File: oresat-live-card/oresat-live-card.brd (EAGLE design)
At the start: 99.8 x 94.6 mm, 323 parts, among them J1 ORESAT-DEBUG-CONNECTOR-CARD, J100 DM3BT-DSF-PEJS, J102 FTSH-105-XX-X-DV-K, J2 SM06B-SRSS-TB(LF)(SN), J4 TFM-120-01-L-D-RA, Q1 MMBT2907, Q2 PMV45EN, Q3 DMP2240UDM, Q4 PMV45EN, Q5 MOSFET-PCH-SOT23-6, Q6 MOSFET-PCH-SOT23-6, U1 RCLAMP0504FB, U10 TLVH431, U11 TCAN330, U12 MIC842LYC5, U13 MIC842LYC5, U14 MAX4211FETE, U15 TPS62112, U16 MAX7310ATE, U17 25AAXX, U18 RCLAMP0504FB, U19 TQP9111, U2 TPS2051CDBVR, U3 THGBMJG7C2LBAU8, U4 SN74LVC1G07DCK, U5 TPS62112, U6 SN74LVC1G32QDBVRQ1, U7 OSD3358-512M-BSM, U8 MIC94090YC6-TR, Y1 24MHz, Y2 ABS07-32.768KHZ-T

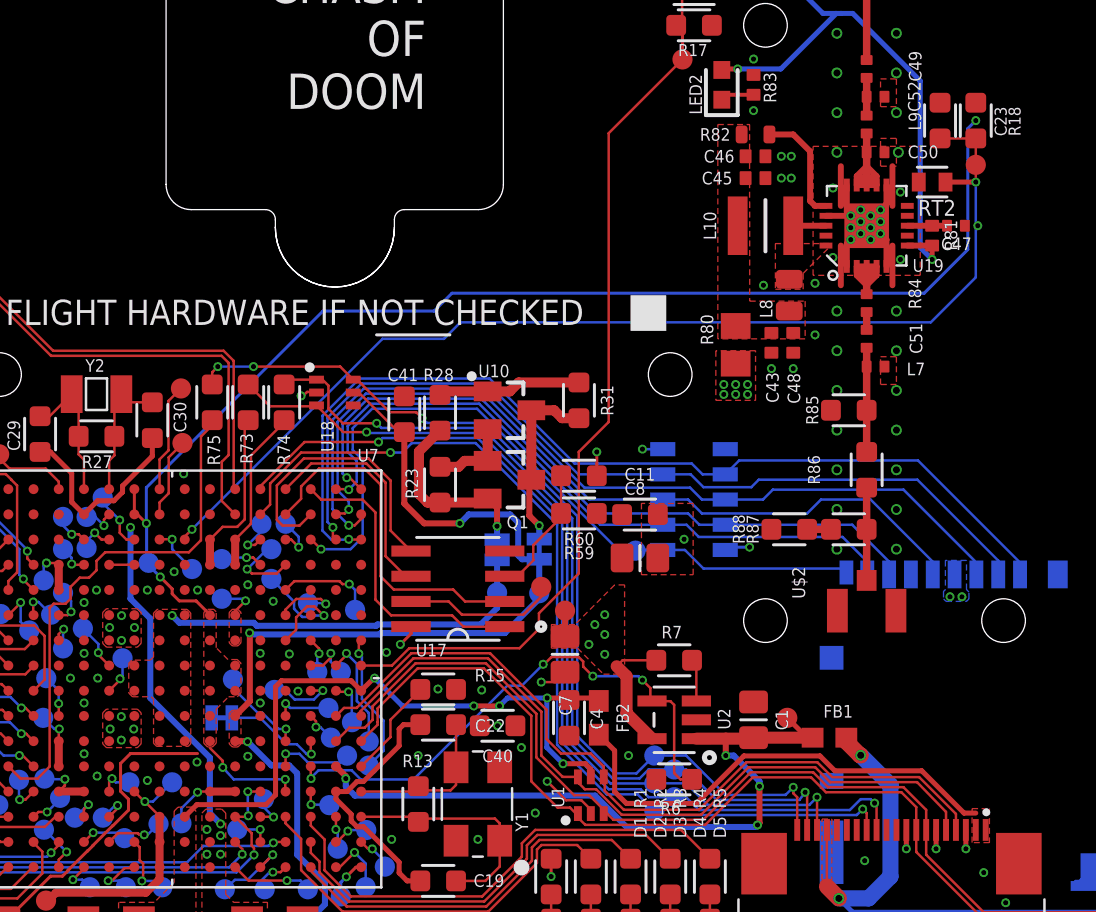
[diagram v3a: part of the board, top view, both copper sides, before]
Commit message: modified thermistor routing to not go though vias after it was moved
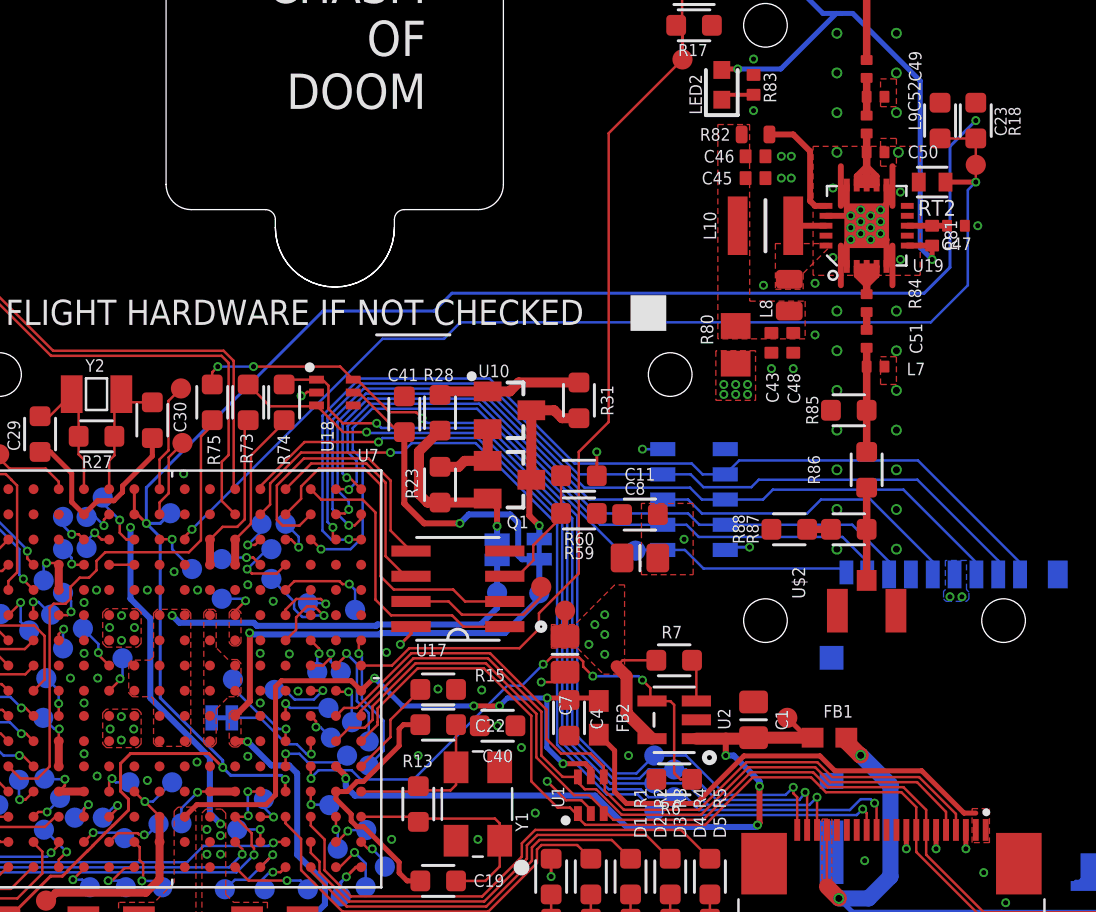
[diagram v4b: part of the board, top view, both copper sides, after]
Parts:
- moved TP171 2.73 mm to (41.6, 25.9)
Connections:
- new net 1.8V-A: C24.1, C25.1, C26.1, TP171.P$1, TP8.P$1, U7.A7, U7.B7, U7.N13
- net 1.8V: no longer C24.1, C25.1, C26.1, TP171.P$1, TP8.P$1, U7.A7, U7.B7, U7.N13
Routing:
- net 1.8V-A: track 0.00 -> 96.2 mm, vias 0 -> 4
- net 1.8V: track 86.8 -> 0.00 mm, vias 5 -> 0
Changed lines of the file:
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@@
 <layer number="13" name="Route13" color="4" fill="5" visible="no" active="no"/>
 <layer number="14" name="Route14" color="1" fill="6" visible="no" active="no"/>
-<layer number="15" name="Route15" color="14" fill="1" visible="no" active="yes"/>
-<layer number="16" name="Bottom" color="1" fill="1" visible="no" active="yes"/>
+<layer number="15" name="Route15" color="14" fill="1" visible="yes" active="yes"/>
+<layer number="16" name="Bottom" color="1" fill="1" visible="yes" active="yes"/>
 <layer number="17" name="Pads" color="2" fill="1" visible="yes" active="yes"/>
 <layer number="18" name="Vias" color="2" fill="1" visible="yes" active="yes"/>
@@
 <layer number="20" name="Dimension" color="15" fill="1" visible="yes" active="yes"/>
 <layer number="21" name="tPlace" color="7" fill="1" visible="yes" active="yes"/>
-<layer number="22" name="bPlace" color="7" fill="1" visible="no" active="yes"/>
+<layer number="22" name="bPlace" color="7" fill="1" visible="yes" active="yes"/>
 <layer number="23" name="tOrigins" color="15" fill="1" visible="yes" active="yes"/>
-<layer number="24" name="bOrigins" color="15" fill="1" visible="no" active="yes"/>
+<layer number="24" name="bOrigins" color="15" fill="1" visible="yes" active="yes"/>
 <layer number="25" name="tNames" color="7" fill="1" visible="no" active="yes"/>
 <layer number="26" name="bNames" color="7" fill="1" visible="no" active="yes"/>
 <layer number="27" name="tValues" color="7" fill="1" visible="no" active="yes"/>
 <layer number="28" name="bValues" color="7" fill="1" visible="no" active="yes"/>
-<layer number="29" name="tStop" color="7" fill="3" visible="yes" active="yes"/>
+<layer number="29" name="tStop" color="7" fill="3" visible="no" active="yes"/>
 <layer number="30" name="bStop" color="7" fill="6" visible="no" active="yes"/>
 <layer number="31" name="tCream" color="7" fill="4" visible="no" active="yes"/>
@@
 <layer number="50" name="dxf" color="61" fill="1" visible="no" active="yes"/>
 <layer number="51" name="tDocu" color="7" fill="1" visible="yes" active="yes"/>
-<layer number="52" name="bDocu" color="7" fill="1" visible="no" active="yes"/>
+<layer number="52" name="bDocu" color="7" fill="1" visible="yes" active="yes"/>
 <layer number="53" name="tGND_GNDA" color="7" fill="9" visible="no" active="no"/>
 <layer number="54" name="bGND_GNDA" color="1" fill="9" visible="no" active="no"/>
@@
 <element name="TP102" library="SparkFun-Connectors" package="PAD.03X.04" value="TEST-POINT3X4" x="48.5375" y="6.9625" smashed="yes" rot="MR0"/>
 <element name="TP112" library="SparkFun-Connectors" package="PAD.03X.04" value="TEST-POINT3X4" x="66" y="13.7" smashed="yes" rot="MR180"/>
-<element name="TP171" library="SparkFun-Connectors" package="PAD.03X.04" value="TEST-POINT3X4" x="40.5125" y="23.4125" smashed="yes" rot="MR0"/>
+<element name="TP171" library="SparkFun-Connectors" package="PAD.03X.04" value="TEST-POINT3X4" x="41.6125" y="25.9125" smashed="yes" rot="MR0"/>
 <element name="TP138" library="SparkFun-Connectors" package="PAD.03X.04" value="TEST-POINT3X4" x="49.7" y="14.6" smashed="yes" rot="MR0"/>
 <element name="JP100" library="SparkFun-Jumpers" package="SMT-JUMPER_2_NC_TRACE_SILK" value="JUMPER-SMT_2_NC_TRACE_SILK" x="44.2" y="15.6" smashed="yes" rot="MR0">
@@
 <wire x1="52.3" y1="34.7" x2="55.4" y2="34.7" width="0.127" layer="16"/>
 <wire x1="55.4" y1="34.7" x2="56.2329" y2="35.5329" width="0.127" layer="16"/>
-<wire x1="79.9329" y1="35.5329" x2="82.2" y2="37.8" width="0.127" layer="16"/>
-<wire x1="82.2" y1="37.8" x2="82.2" y2="42.6" width="0.127" layer="16"/>
+<wire x1="79.9329" y1="35.5329" x2="81.8" y2="37.4" width="0.127" layer="16"/>
+<wire x1="81.8" y1="42.2" x2="81.8" y2="37.4" width="0.127" layer="16"/>
+<wire x1="81.8" y1="42.2" x2="82.2" y2="42.6" width="0.127" layer="16"/>
 <wire x1="56.2329" y1="35.5329" x2="79.9329" y2="35.5329" width="0.127" layer="16"/>
 <wire x1="82.2" y1="43.46875" x2="82.2" y2="42.6" width="0.127" layer="1"/>
@@
 </signal>
 <signal name="1.8V">
+<contactref element="R18" pad="1"/>
+</signal>
+<signal name="1.8V-A">
 <contactref element="U7" pad="A7"/>
 <contactref element="C26" pad="1"/>
@@
 <wire x1="30.125" y1="5.525" x2="31.725" y2="5.525" width="0.1524" layer="1"/>
 <wire x1="31.725" y1="5.525" x2="33.325" y2="5.525" width="0.1524" layer="1"/>
-<wire x1="43.605" y1="20.795" x2="42.9082" y2="21.4918" width="0.1524" layer="1"/>
-<wire x1="42.9082" y1="21.4918" x2="42.05911875" y2="21.4918" width="0.1524" layer="1"/>
-<via x="41.1" y="22.7" extent="1-16" drill="0.254"/>
-<wire x1="40.5125" y1="23.4125" x2="40.5125" y2="23.2875" width="0.1524" layer="16"/>
-<wire x1="40.5125" y1="23.2875" x2="41.1" y2="22.7" width="0.1524" layer="16"/>
-<wire x1="40.4125" y1="25.3875" x2="40.4125" y2="23.5125" width="0.1524" layer="16"/>
-<wire x1="40.5125" y1="23.4125" x2="40.4125" y2="23.5125" width="0.1524" layer="16"/>
-<wire x1="40.4125" y1="25.3875" x2="40.4" y2="25.4" width="0.1524" layer="16"/>
+<wire x1="41.6125" y1="25.9125" x2="41.6125" y2="25.7875" width="0.1524" layer="16"/>
+<wire x1="41.6125" y1="25.9125" x2="41.1" y2="25.4" width="0.1524" layer="16"/>
+<wire x1="41.1" y1="25.4" x2="40.4" y2="25.4" width="0.1524" layer="16"/>
 <via x="40.4" y="25.4" extent="1-16" drill="0.254"/>
 <wire x1="39.795" y1="25.855" x2="39.945" y2="25.855" width="0.1524" layer="1"/>
 <wire x1="39.945" y1="25.855" x2="40.4" y2="25.4" width="0.1524" layer="1"/>
 <wire x1="39.795" y1="25.855" x2="39.795" y2="27.125" width="0.1524" layer="1"/>
-<wire x1="41.7" y1="22.1" x2="41.1" y2="22.7" width="0.1524" layer="1"/>
-<wire x1="41.7" y1="22.1" x2="41.7" y2="21.85091875" width="0.1524" layer="1"/>
-<wire x1="42.05911875" y1="21.4918" x2="41.7" y2="21.85091875" width="0.1524" layer="1"/>
-<wire x1="42.98" y1="13.8" x2="39.6" y2="13.8" width="0.1524" layer="1"/>
-<wire x1="39.6" y1="13.8" x2="39.1" y2="13.3" width="0.1524" layer="1"/>
+<wire x1="39.1" y1="13.3" x2="39.6" y2="13.8" width="0.1524" layer="1"/>
 <wire x1="39.1" y1="12.7169125" x2="39.10055" y2="12.7163625" width="0.1524" layer="1"/>
 <wire x1="39.10055" y1="12.7163625" x2="39.10055" y2="12.3586375" width="0.1524" layer="1"/>
@@
 <wire x1="55.8" y1="37" x2="79.6" y2="37" width="0.1524" layer="16"/>
 <wire x1="54.9" y1="36.1" x2="55.8" y2="37" width="0.1524" layer="16"/>
-<wire x1="79.6" y1="37" x2="81.8" y2="39.2" width="0.1524" layer="16"/>
-<wire x1="81.8" y1="39.2" x2="81.8" y2="45.3" width="0.1524" layer="16"/>
-<wire x1="81.8" y1="45.3" x2="82.2" y2="45.7" width="0.1524" layer="16"/>
+<wire x1="79.6" y1="37" x2="80.9" y2="38.3" width="0.1524" layer="16"/>
+<wire x1="80.9" y1="38.3" x2="80.9" y2="44.4" width="0.1524" layer="16"/>
+<wire x1="80.9" y1="44.4" x2="82.2" y2="45.7" width="0.1524" layer="16"/>
 <via x="82.2" y="45.7" extent="1-16" drill="0.254"/>
-<contactref element="R18" pad="1"/>
 <contactref element="U7" pad="N13"/>
 <contactref element="TP8" pad="P$1"/>
-<wire x1="47.415" y1="11.885" x2="47.4" y2="11.9" width="0.127" layer="1"/>
-<wire x1="47.4" y1="11.9" x2="47.4" y2="12.5" width="0.127" layer="1"/>
-<via x="47.4" y="12.5" extent="1-16" drill="0.254"/>
-<wire x1="47.4" y1="12.5" x2="44.8" y2="12.5" width="0.127" layer="16"/>
-<wire x1="44.8" y1="12.5" x2="44.25" y2="13.1" width="0.127" layer="16"/>
 <via x="44.25" y="13.1" extent="1-16" drill="0.254"/>
-<wire x1="44.25" y1="13.4329625" x2="43.605" y2="14.0779625" width="0.127" layer="1"/>
-<wire x1="44.25" y1="13.4329625" x2="44.25" y2="13.1" width="0.127" layer="1"/>
-<wire x1="82.2" y1="45.7" x2="82.2" y2="46.6" width="0" layer="19" extent="1-1"/>
-<wire x1="43.605" y1="14.0779625" x2="43.605" y2="20.795" width="0" layer="19" extent="1-1"/>
-<wire x1="42.98" y1="13.8" x2="43.605" y2="14.0779625" width="0" layer="19" extent="1-1"/>
+<wire x1="43.55" y1="13.8" x2="44.25" y2="13.1" width="0.1524" layer="1"/>
+<wire x1="39.6" y1="13.8" x2="43.55" y2="13.8" width="0.1524" layer="1"/>
+<wire x1="47.415" y1="11.885" x2="47.4" y2="11.9" width="0.1524" layer="1"/>
+<wire x1="47.4" y1="11.9" x2="47.4" y2="12.5" width="0.1524" layer="1"/>
+<via x="47.4" y="12.5" extent="1-16" drill="0.254"/>
+<wire x1="44.25" y1="13.1" x2="44.65" y2="12.7" width="0.1524" layer="16"/>
+<wire x1="47.2" y1="12.7" x2="47.4" y2="12.5" width="0.1524" layer="16"/>
+<wire x1="47.2" y1="12.7" x2="44.65" y2="12.7" width="0.1524" layer="16"/>
+<wire x1="44.25" y1="13.1" x2="44.25" y2="13.4529" width="0.1524" layer="16"/>
+<wire x1="44.25" y1="13.4529" x2="41.1" y2="16.6029" width="0.1524" layer="16"/>
+<wire x1="41.1" y1="24.7" x2="40.4" y2="25.4" width="0.1524" layer="16"/>
+<wire x1="41.1" y1="16.6029" x2="41.1" y2="24.7" width="0.1524" layer="16"/>
 <wire x1="-0.5" y1="-7.5" x2="30.125" y2="5.525" width="0" layer="19" extent="1-1"/>
 </signal>

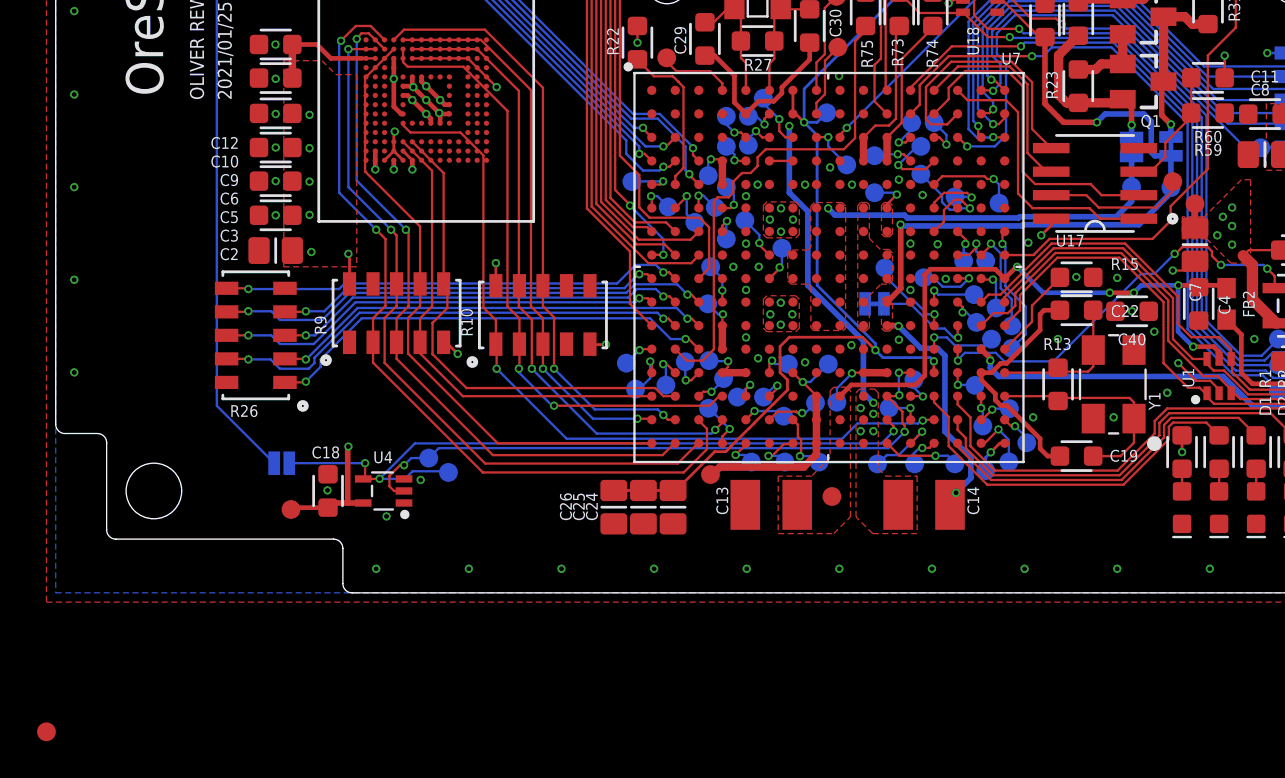
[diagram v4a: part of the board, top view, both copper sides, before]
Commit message: Fixed the I2C0 ESD protection following Oliver R's instructions
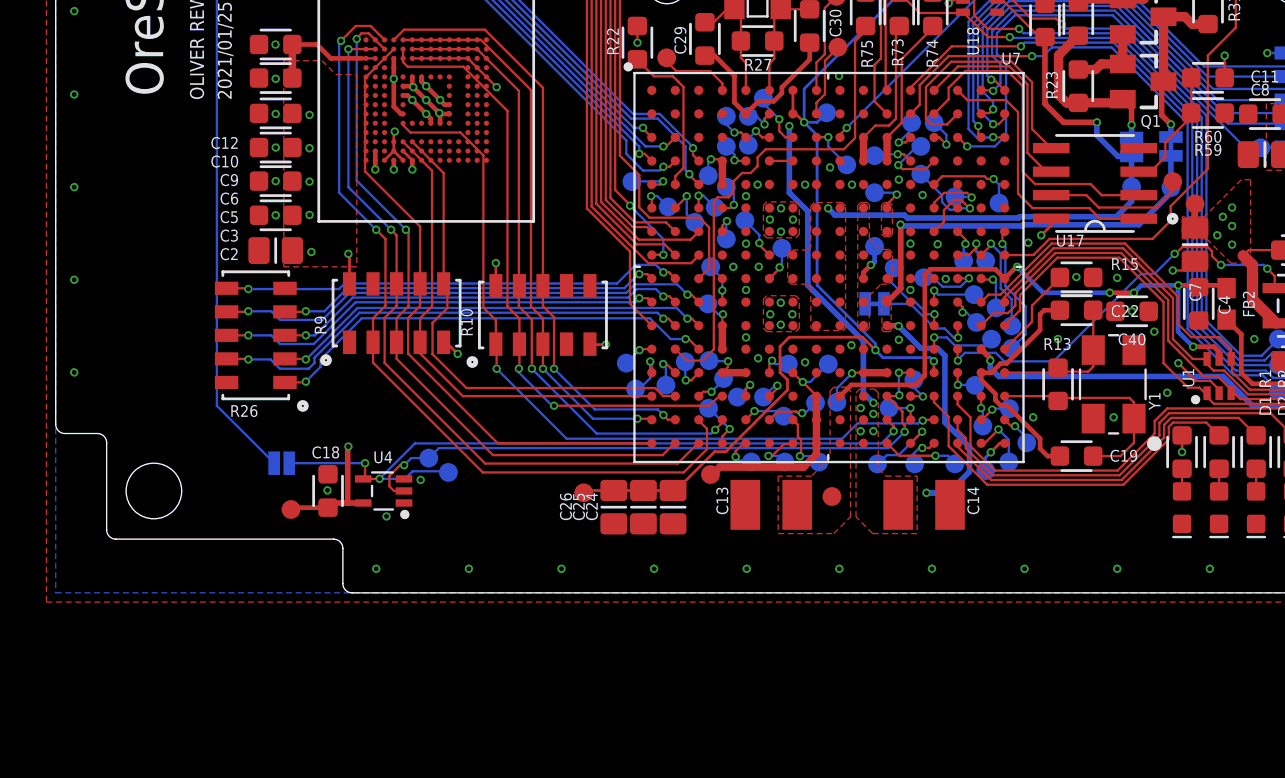
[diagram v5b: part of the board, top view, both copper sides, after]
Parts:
- added TP9: TEST-POINT3X4, SparkFun-Connectors:PAD.03X.04
- moved TP8 31.7 mm to (28.5, 5.40)
- moved TP144 0.50 mm to (45.3, 17.5)
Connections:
- removed net N$26: JP101.1, TP165.P$1, U7.F8, U7.F9, U7.G8, U7.G9, U7.H7, U7.H8, U7.H9, U7.J7, U7.J8, U7.J9, U7.K8, U7.K9, U7.L8, U7.L9
- new net N$53: C18.1, JP104.1, TP14.P$1, TP164.P$1, U4.5, U7.K11, U7.L11
- net 3.3VA: now also JP101.1, TP165.P$1, U7.F8, U7.F9, U7.G8, U7.G9, U7.H7, U7.H8, U7.H9, U7.J7, U7.J8, U7.J9, U7.K8, U7.K9, U7.L8, U7.L9; no longer C18.1, JP104.1, TP14.P$1, TP164.P$1, U4.5, U7.K11, U7.L11
- net N$3: now also TP9.P$1
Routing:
- net N$53: track 0.00 -> 75.8 mm, vias 0 -> 4
- net 3.3VA: track 91.4 -> 32.7 mm, vias 5 -> 2
- net N$26: track 19.4 -> 0.00 mm, vias 1 -> 0
- net N$3: track 0.00 -> 2.01 mm, vias 0 -> 1
- net 1.8V-A: track 96.2 -> 97.8 mm
- added copper zone on layer 1, net N$3
- added copper zone on layer 1, net N$53
- removed copper zone on layer 1, net 1.8V-L
- removed copper zone on layer 1, net N$26
